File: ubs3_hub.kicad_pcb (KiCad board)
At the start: 4 copper layers, 85 x 37.5 mm, 64 parts, among them J1 USB_C_Receptacle, J2 USB_C_Receptacle, J3 USB3_A, J4 USB3_A, J5 USB3_A, U2 CH213K, U3 CH217K, U4 CH217K, U5 CH217K, U6 CH217K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

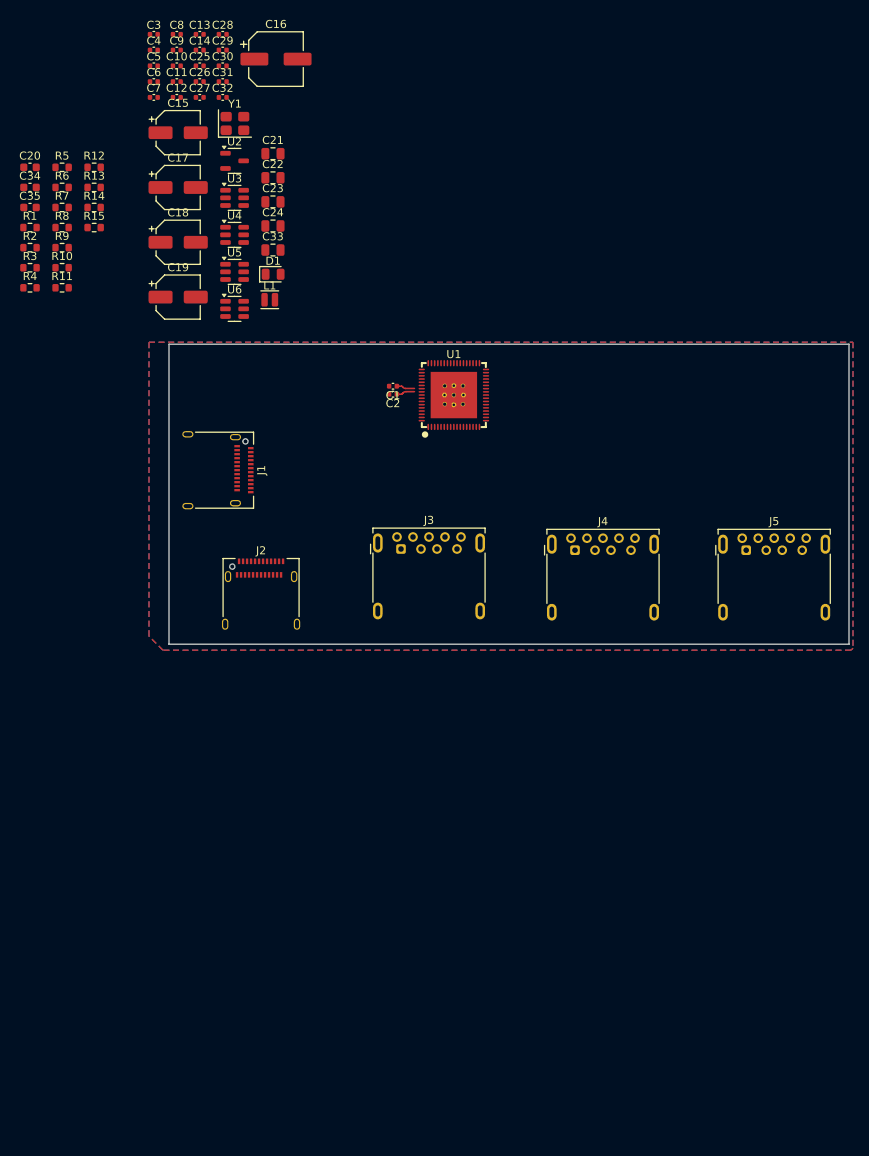
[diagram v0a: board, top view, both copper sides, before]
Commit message: placement finished, power layout ok
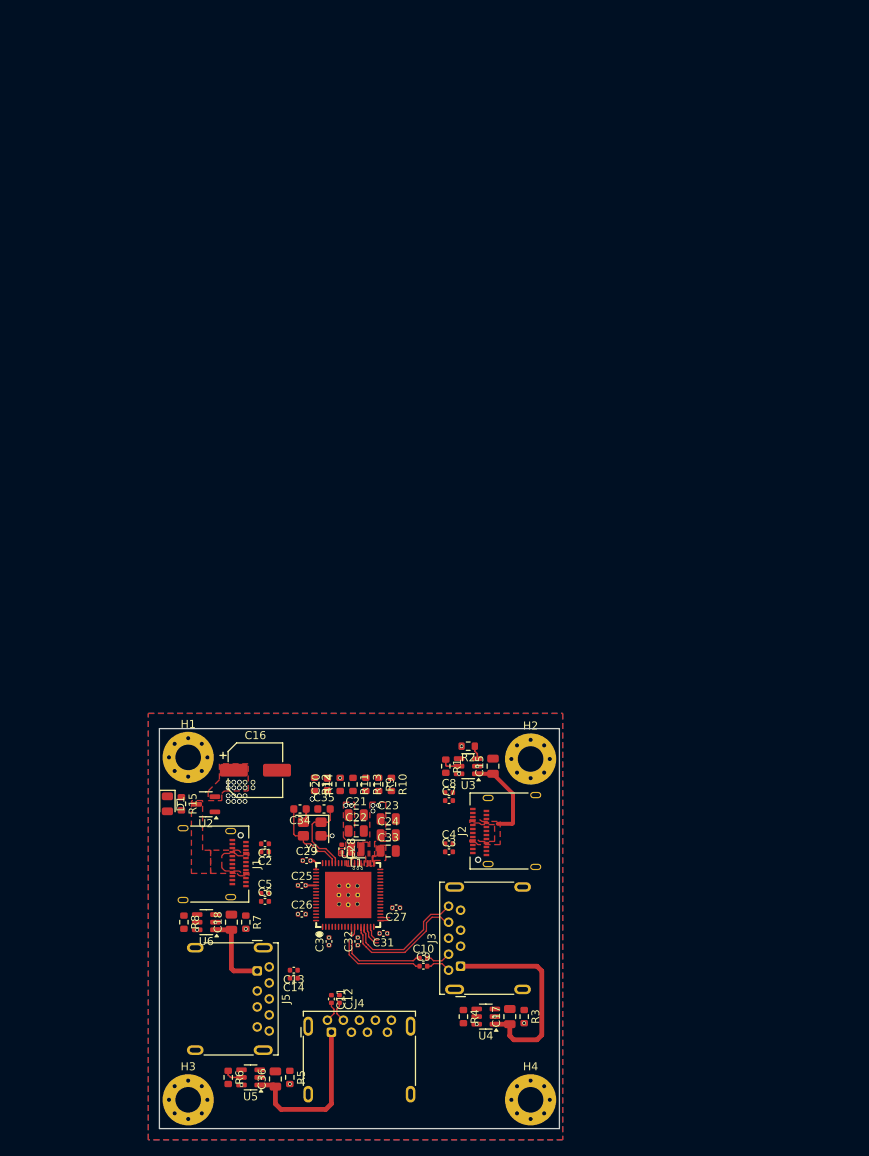
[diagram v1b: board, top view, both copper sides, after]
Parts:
- removed C19: 22u/25V, Capacitor_SMD:CP_Elec_5x5.4
- added C36: 22u, Capacitor_SMD:C_0805_2012Metric, F.Cu at (86.3, 163.6)
- added H1: MountingHole_Pad, MountingHole:MountingHole_3.2mm_M3_Pad_Via, F.Cu at (75.4, 123.4)
- added H2: MountingHole_Pad, MountingHole:MountingHole_3.2mm_M3_Pad_Via, F.Cu at (118.2, 123.6)
- added H3: MountingHole_Pad, MountingHole:MountingHole_3.2mm_M3_Pad_Via, F.Cu at (75.4, 166.2)
- added H4: MountingHole_Pad, MountingHole:MountingHole_3.2mm_M3_Pad_Via, F.Cu at (118.2, 166.2)
- C15, C17, C18: value 22u/25V -> 22u; footprint Capacitor_SMD:CP_Elec_5x5.4 -> Capacitor_SMD:C_0805_2012Metric
- moved C9 118.6 mm to (104.8, 149.5)
- moved C13 117.6 mm to (88.6, 150.0), turned to 180 degrees
- moved R5 117.3 mm to (88.1, 163.4), turned to -90 degrees
- moved C14 116.6 mm to (88.6, 151.0), turned to 180 degrees
- moved C11 116.3 mm to (93.3, 153.6), turned to -90 degrees
- moved C10 115.7 mm to (104.8, 148.5)
- moved C12 114.5 mm to (94.3, 153.6), turned to -90 degrees
- moved R6 113.2 mm to (80.4, 163.4), turned to -90 degrees
- moved R3 112.2 mm to (117.4, 155.8), turned to -90 degrees
- moved C17 111.6 mm to (115.6, 155.8), turned to 90 degrees
- moved C30 110.2 mm to (93.0, 146.4), turned to 90 degrees
- moved C3 108.6 mm to (108.0, 135.2)
- moved C31 108.3 mm to (99.8, 145.4), turned to 180 degrees
- moved C32 106.8 mm to (96.6, 146.4), turned to 90 degrees
- moved R4 106.0 mm to (109.8, 155.8), turned to -90 degrees
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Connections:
- C18 pad 1: VBUS_OUT3 -> VBUS_OUT4
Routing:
- net VBUS_OUT2: track 0.00 -> 26.2 mm
- net VBUS_OUT3: track 0.00 -> 20.7 mm
- net /P2_SS_RX_N: track 0.00 -> 16.0 mm
- net /P2_SS_RX_P: track 0.00 -> 15.6 mm
- net /P2_SS_TXC_P: track 0.00 -> 12.4 mm
- net /P2_SS_TXC_N: track 0.00 -> 11.5 mm
- net VBUS_OUT1: track 0.00 -> 11.1 mm
- net Net-(U1-XO): track 0.00 -> 10.4 mm
- net Net-(U1-XI): track 0.00 -> 10.2 mm
- net VBUS_OUT4: track 0.00 -> 10.2 mm
- net GND: track 0.00 -> 3.19 mm, vias 0 -> 24
- net /P2_SS_TX_P: track 0.00 -> 3.14 mm
- net /P2_SS_TX_N: track 0.00 -> 3.14 mm
- net +1V2: track 0.00 -> 2.94 mm, vias 0 -> 9
- net /P1_SS_TXC_N: track 0.00 -> 2.85 mm
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- added copper zone on F.Cu, net +1V2
- added copper zone on In3.Cu, net +1V2
- added copper zone on F.Cu, net +3.3V
- added copper zone on F.Cu, net +5V
- added copper zone on In3.Cu, net +5V
- added copper zone on F.Cu, net /VSW
- added copper zone on In4.Cu, net GND
- added copper zone on F.Cu, net VBUS
- added copper zone on F.Cu, net VBUS_OUT1
- removed copper zone on In2.Cu, net GND
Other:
- board size 85 x 37.5 mm -> 50 x 50 mm
- copper layers 4 -> 6

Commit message: Layout in progress
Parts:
- moved C6 11.7 mm to (85.0, 129.7), turned to 180 degrees
- moved C5 9.70 mm to (85.0, 130.7), turned to 180 degrees
- moved C13 1.10 mm to (88.6, 151.1)
- moved C3 1.10 mm to (108.0, 134.1)
- moved C10 1.00 mm to (104.8, 149.5)
- moved C11 1.00 mm to (94.3, 153.6)
- moved C12 1.00 mm to (93.3, 153.6)
- moved C9 1.00 mm to (104.8, 148.5)
- moved C34 0.92 mm to (90.2, 129.5)
- moved C35 0.92 mm to (93.2, 129.5)
- moved Y1 0.92 mm to (91.8, 132.0)
- moved C14 0.90 mm to (88.6, 150.1)
- moved C4 0.90 mm to (108.0, 135.1)
- moved C1 0.41 mm to (84.6, 134.3)
- moved C2 0.41 mm to (84.6, 135.3)
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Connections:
- C10 pad 1: /P2_SS_TXC_N -> /P2_SS_TXC_P
- C10 pad 2: /P2_SS_TX_N -> /P2_SS_TX_P
- C11 pad 1: /P3_SS_TXC_P -> /P3_SS_TXC_N
- C11 pad 2: /P3_SS_TX_P -> /P3_SS_TX_N
- C12 pad 1: /P3_SS_TXC_N -> /P3_SS_TXC_P
- C12 pad 2: /P3_SS_TX_N -> /P3_SS_TX_P
- C13 pad 1: /P4_SS_TXC_P -> /P4_SS_TXC_N
- C13 pad 2: /P4_SS_TX_P -> /P4_SS_TX_N
- C14 pad 1: /P4_SS_TXC_N -> /P4_SS_TXC_P
- C14 pad 2: /P4_SS_TX_N -> /P4_SS_TX_P
- C3 pad 1: /P1_SS_TXC_P -> /P1_SS_TXC_N
- C3 pad 2: /P1_SS_TX_P -> /P1_SS_TX_N
- C4 pad 1: /P1_SS_TXC_N -> /P1_SS_TXC_P
- C4 pad 2: /P1_SS_TX_N -> /P1_SS_TX_P
- C5 pad 1: /UPC_SS_TXC_P -> /UPC_SS_TXC_N
- C5 pad 2: /UPC_SS_TX_P -> /UPC_SS_TX_N
- C6 pad 1: /UPC_SS_TXC_N -> /UPC_SS_TXC_P
- C6 pad 2: /UPC_SS_TX_N -> /UPC_SS_TX_P
- C9 pad 1: /P2_SS_TXC_P -> /P2_SS_TXC_N
- C9 pad 2: /P2_SS_TX_P -> /P2_SS_TX_N
- U1 pad 1: /P3_SS_TXC_N -> /P3_SS_TXC_P
- U1 pad 10: /P2_SS_TXC_N -> /P2_SS_TXC_P
- U1 pad 11: /P2_SS_TXC_P -> /P2_SS_TXC_N
- U1 pad 15: /P1_SS_TXC_N -> /P1_SS_TXC_P
- U1 pad 16: /P1_SS_TXC_P -> /P1_SS_TXC_N
- U1 pad 2: /P3_SS_TXC_P -> /P3_SS_TXC_N
- U1 pad 20: /P1C_SS_RX_P -> /P1C_SS_RX_N
- U1 pad 21: /P1C_SS_RX_N -> /P1C_SS_RX_P
- U1 pad 4: /P3_SS_RX_N -> /P3_SS_RX_P
- U1 pad 5: /P3_SS_RX_P -> /P3_SS_RX_N
- U1 pad 50: /UPC_SS_TXC_N -> /UPC_SS_TXC_P
- U1 pad 51: /UPC_SS_TXC_P -> /UPC_SS_TXC_N
- U1 pad 55: /UP_SS_RX_P -> /UP_SS_RX_N
- U1 pad 56: /UP_SS_RX_N -> /UP_SS_RX_P
- U1 pad 64: /P4_SS_TXC_N -> /P4_SS_TXC_P
- U1 pad 65: /P4_SS_TXC_P -> /P4_SS_TXC_N
- U1 pad 67: /P4_SS_RX_N -> /P4_SS_RX_P
- U1 pad 68: /P4_SS_RX_P -> /P4_SS_RX_N
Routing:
- net /P3_HS_N: track 0.00 -> 37.0 mm, vias 0 -> 1
- net /P2_HS_P: track 0.00 -> 36.4 mm, vias 0 -> 1
- net /P3_HS_P: track 0.00 -> 35.8 mm, vias 0 -> 1
- net /P2_HS_N: track 0.00 -> 34.6 mm, vias 0 -> 1
- net /P1_SS_RX_N: track 1.19 -> 27.8 mm, vias 0 -> 2
- net /P1_SS_RX_P: track 1.19 -> 26.8 mm, vias 0 -> 2
- net /P4_HS_P: track 0.00 -> 25.6 mm, vias 0 -> 1
- net /P4_HS_N: track 0.00 -> 24.4 mm, vias 0 -> 1
- net /UP_SS_RX_N: track 0.00 -> 22.5 mm
- net /P1_HS_N: track 0.00 -> 21.7 mm, vias 0 -> 4
- net /UP_SS_RX_P: track 0.00 -> 21.3 mm
- net /UPC_SS_TX_P: track 0.00 -> 20.6 mm
- net /P1C_SS_RX_P: track 0.00 -> 20.3 mm
- net /P1C_SS_RX_N: track 0.00 -> 20.3 mm
- net /P1_HS_P: track 0.00 -> 20.0 mm, vias 0 -> 2
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- added copper zone on In3.Cu, net VBUS

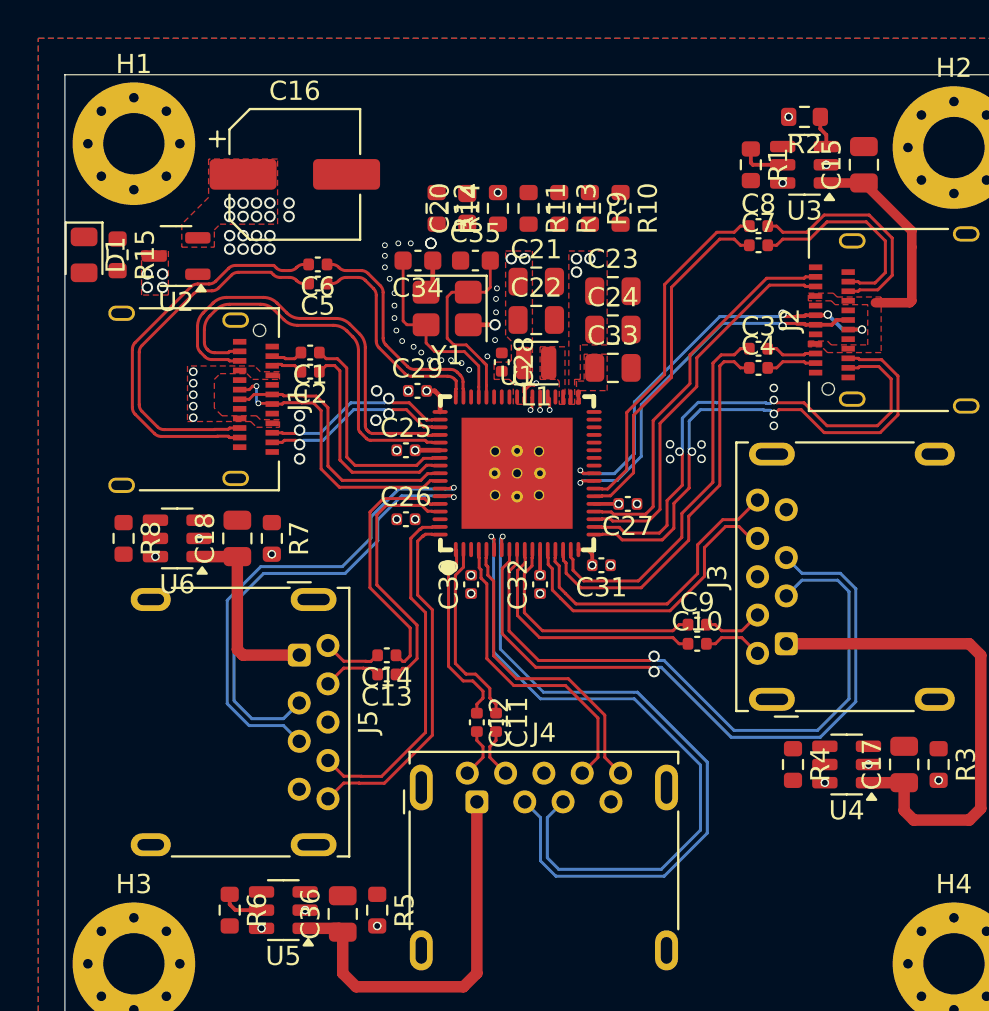
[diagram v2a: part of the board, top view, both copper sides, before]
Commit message: updated layout
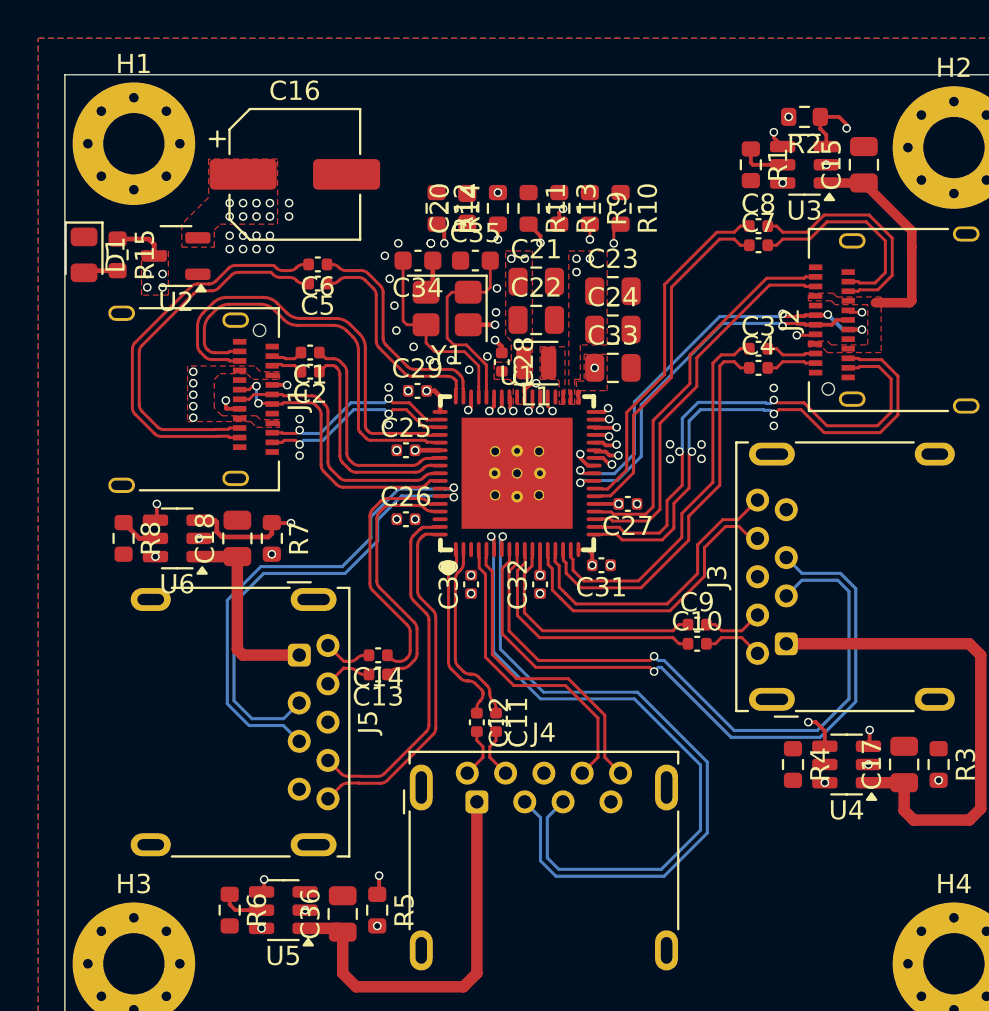
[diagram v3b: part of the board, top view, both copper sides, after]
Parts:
- moved C13 0.45 mm to (88.2, 151.1)
- moved C14 0.45 mm to (88.2, 150.1)
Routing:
- net +3.3V: track 0.00 -> 156.5 mm, vias 5 -> 6
- net /~{OVRCUR1}: track 1.68 -> 66.9 mm, vias 0 -> 2
- net /UP_CC2: track 0.77 -> 42.7 mm, vias 1 -> 3
- net /~{PWREN3}: track 0.00 -> 40.3 mm, vias 0 -> 2
- net /UP_CC1: track 1.10 -> 36.0 mm, vias 1 -> 3
- net /~{PWREN1}: track 0.00 -> 34.6 mm, vias 0 -> 2
- net /~{OVRCUR3}: track 0.00 -> 32.8 mm, vias 0 -> 2
- net /~{PWREN4}: track 0.00 -> 27.3 mm, vias 0 -> 2
- net /~{OVRCUR2}: track 0.00 -> 26.3 mm, vias 0 -> 2
- net /~{OVRCUR4}: track 0.00 -> 26.0 mm, vias 0 -> 2
- net /~{PWREN2}: track 0.00 -> 25.0 mm, vias 0 -> 2
- net /P1_CC2: track 0.72 -> 19.9 mm, vias 1 -> 2
- net /P1_CC1: track 0.68 -> 16.9 mm, vias 1 -> 2
- net Net-(U1-SMB_DAT/SDA): track 0.00 -> 13.7 mm, vias 0 -> 2
- net Net-(U1-SUSP/PD_HUB#): track 0.00 -> 13.3 mm, vias 0 -> 2
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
